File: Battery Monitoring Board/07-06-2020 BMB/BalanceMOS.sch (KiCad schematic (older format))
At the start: 7 parts, among them J20 Conn_01x01, Q2 Q_PMOS_GSD

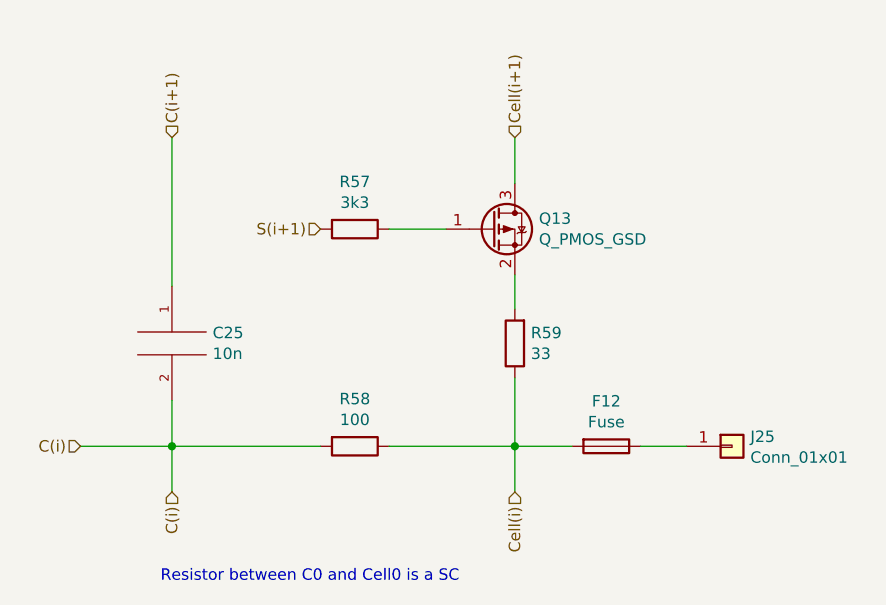
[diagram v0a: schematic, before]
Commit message: BMB wired BMI connector
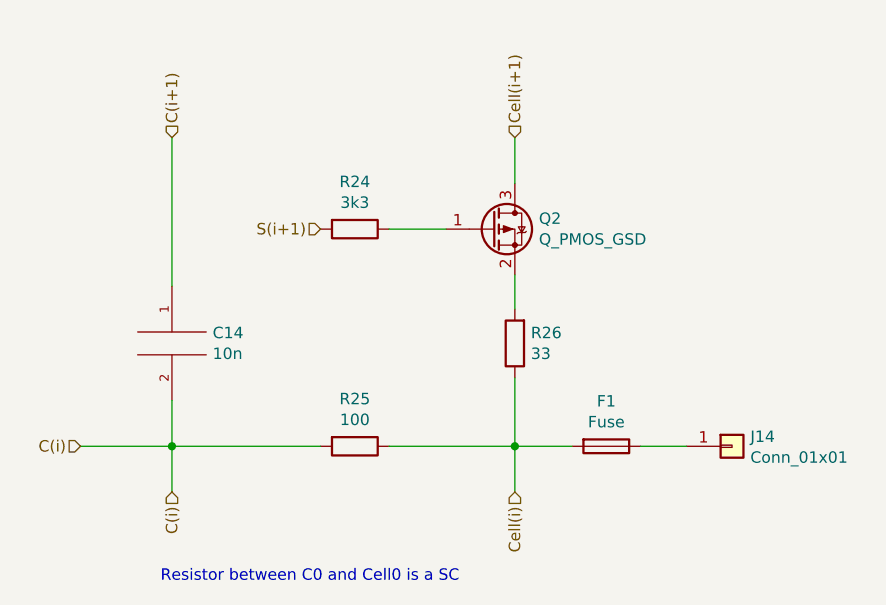
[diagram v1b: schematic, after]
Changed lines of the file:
@@
 $Descr A4 11693 8268
 encoding utf-8
-Sheet 13 13
+Sheet 2 13
 Title ""
 Date ""
@@
 AR Path="/5EABD885/5EA84DC6" Ref="R54"  Part="1"
 AR Path="/5EABD891/5EA84DC6" Ref="R57"  Part="1"
-F 0 "R57" V 5343 3400 50  0000 C CNN
+F 0 "R24" V 5343 3400 50  0000 C CNN
 F 1 "3k3" V 5434 3400 50  0000 C CNN
 F 2 "Resistor_SMD:R_0805_2012Metric" V 5480 3400 50  0001 C CNN
@@
 AR Path="/5EABD885/5EA8547C" Ref="R56"  Part="1"
 AR Path="/5EABD891/5EA8547C" Ref="R59"  Part="1"
-F 0 "R59" H 6180 3854 50  0000 R CNN
+F 0 "R26" H 6180 3854 50  0000 R CNN
 F 1 "33" H 6180 3945 50  0000 R CNN
 F 2 "Resistor_SMD:R_0805_2012Metric" V 6180 3900 50  0001 C CNN
@@
 AR Path="/5EABD885/5EA85C2A" Ref="R55"  Part="1"
 AR Path="/5EABD891/5EA85C2A" Ref="R58"  Part="1"
-F 0 "R58" V 5343 4350 50  0000 C CNN
+F 0 "R25" V 5343 4350 50  0000 C CNN
 F 1 "100" V 5434 4350 50  0000 C CNN
 F 2 "Resistor_SMD:R_0805_2012Metric" V 5480 4350 50  0001 C CNN
@@
 AR Path="/5EABD885/5EA86272" Ref="C24"  Part="1"
 AR Path="/5EABD891/5EA86272" Ref="C25"  Part="1"
-F 0 "C25" H 4928 3946 50  0000 L CNN
+F 0 "C14" H 4928 3946 50  0000 L CNN
 F 1 "10n" H 4928 3855 50  0000 L CNN
 F 2 "Capacitor_SMD:C_0805_2012Metric" H 4750 3900 50  0001 C CNN
@@
 AR Path="/5EABD885/5EA8857A" Ref="F11"  Part="1"
 AR Path="/5EABD891/5EA8857A" Ref="F12"  Part="1"
-F 0 "F12" V 6453 4350 50  0000 C CNN
+F 0 "F1" V 6453 4350 50  0000 C CNN
 F 1 "Fuse" V 6544 4350 50  0000 C CNN
 F 2 "Fuse:Fuse_1206_3216Metric" V 6580 4350 50  0001 C CNN
@@
 AR Path="/5EABD885/5EA63824" Ref="J24"  Part="1"
 AR Path="/5EABD891/5EA63824" Ref="J25"  Part="1"
-F 0 "J25" H 7280 4392 50  0000 L CNN
+F 0 "J14" H 7280 4392 50  0000 L CNN
 F 1 "Conn_01x01" H 7280 4301 50  0000 L CNN
 F 2 "Connector_TE-Connectivity:TE_MATE-N-LOK_1-794374-x_1x01_P4.14mm_Horizontal" H 7200 4350 50  0001 C CNN
@@
 AR Path="/5EABD885/5EAE8C0F" Ref="Q12"  Part="1"
 AR Path="/5EABD891/5EAE8C0F" Ref="Q13"  Part="1"
-F 0 "Q13" H 6355 3446 50  0000 L CNN
+F 0 "Q2" H 6355 3446 50  0000 L CNN
 F 1 "Q_PMOS_GSD" H 6355 3355 50  0000 L CNN
 F 2 "Package_TO_SOT_SMD:SOT-23" H 6350 3500 50  0001 C CNN
